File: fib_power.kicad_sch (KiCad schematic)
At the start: 44 parts, among them U2 TPS56428DDA, U202 TLV75733PDBV, U204 TPS56428DDA, U205 TPS56428DDA

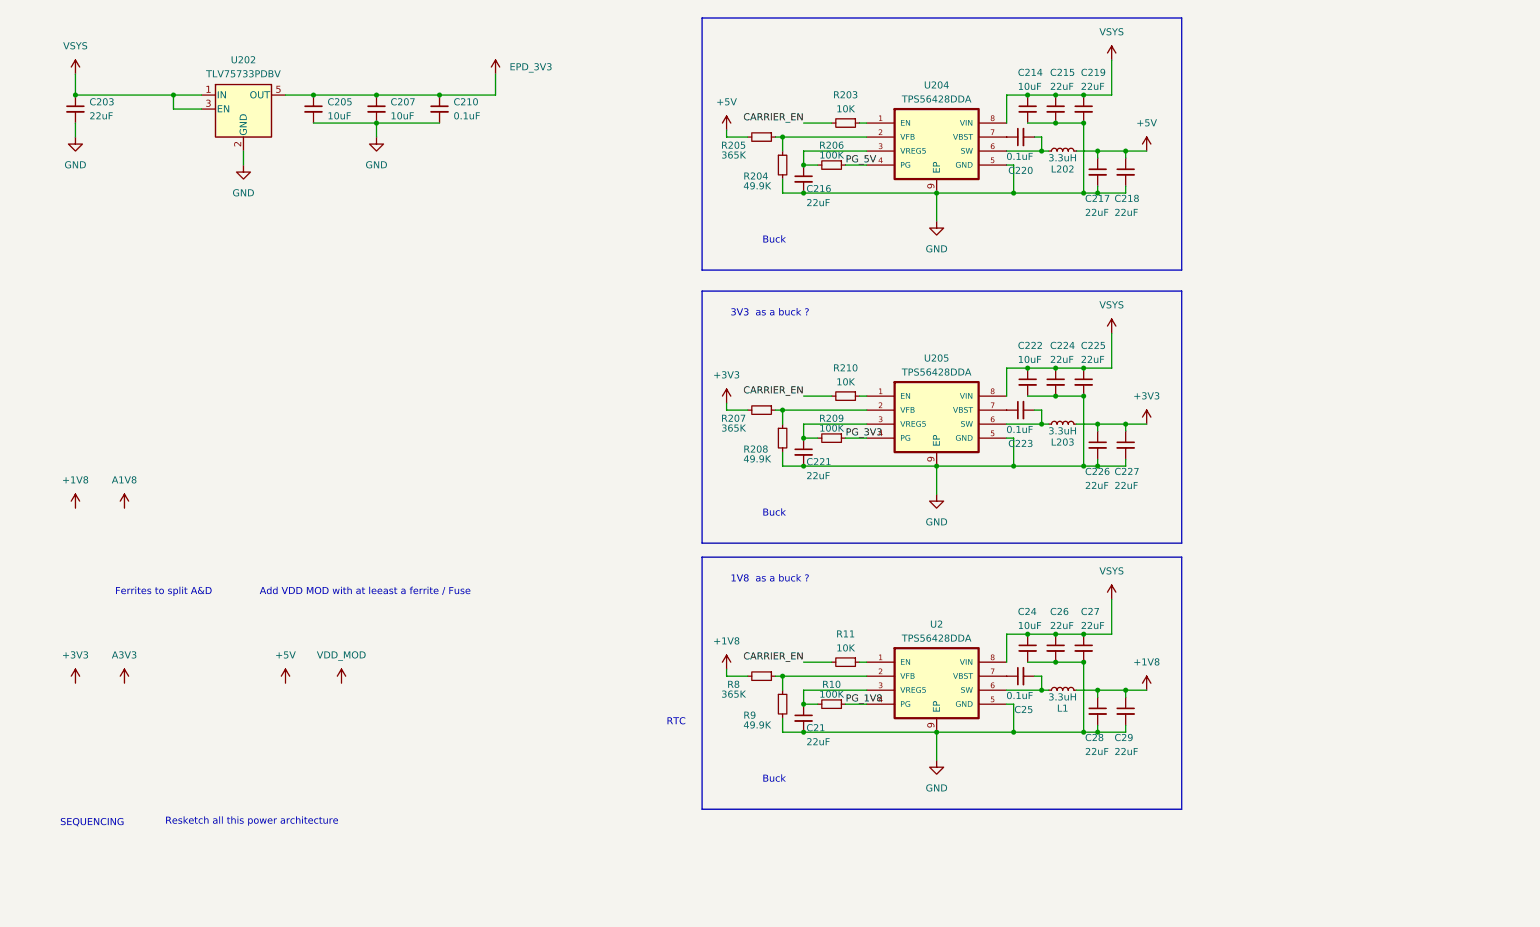
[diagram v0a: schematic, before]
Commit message: replaced 1v8 buck with ldo, added startup circuit, added footprints for eink connectors
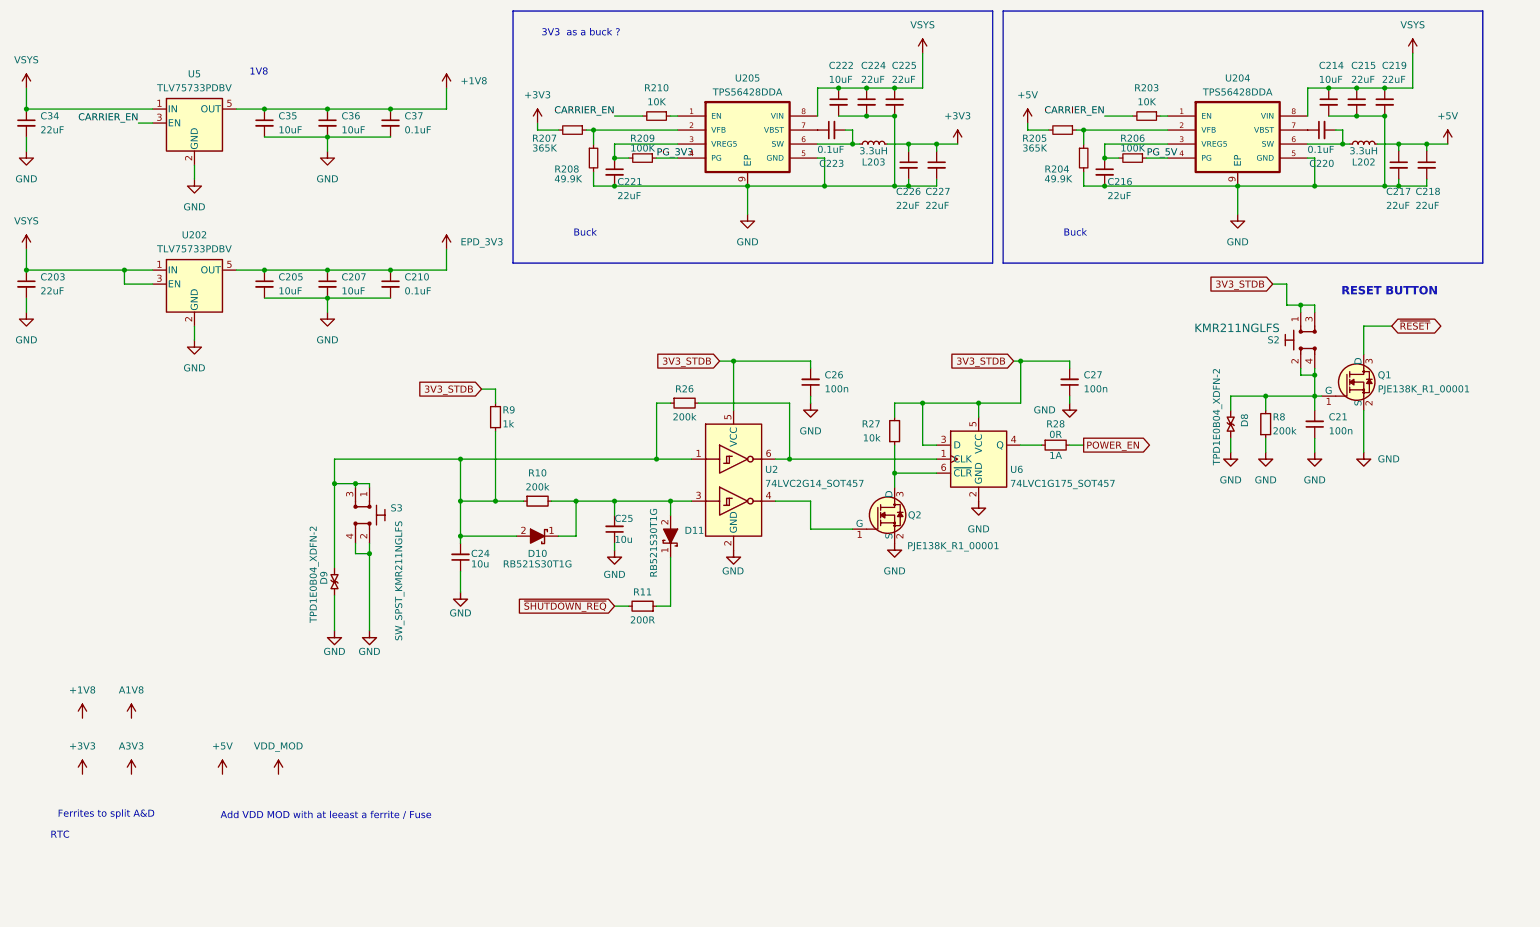
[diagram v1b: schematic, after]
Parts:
- removed C21, C26, C27, C29: 22uF, Capacitor_SMD:C_0805_2012Metric, symbol Device:C_Small
- removed C24: 10uF, Capacitor_SMD:C_0603_1608Metric, symbol Device:C_Small
- removed C25: 0.1uF, Capacitor_SMD:C_0402_1005Metric, symbol Device:C_Small
- removed C28: 22uF, Capacitor_SMD:C_0603_1608Metric, symbol Device:C_Small
- removed L1: 3.3uH, Inductor_SMD:L_Coilcraft_XAL4030-XXX, symbol Device:L_Small
- removed R10: 100K, Resistor_SMD:R_0402_1005Metric, symbol Device:R_Small
- removed R11: 10K, Resistor_SMD:R_0402_1005Metric, symbol Device:R_Small
- removed R8: 365K, Resistor_SMD:R_0402_1005Metric, symbol Device:R_Small
- removed R9: 49.9K, Resistor_SMD:R_0402_1005Metric, symbol Device:R_Small
- removed U2: TPS56428DDA, Fibel2:TPS56428DDA, symbol Fibel2:TPS56428DDA
- added C21, C26, C27: C_100n_0402, antmicro-footprints:C_0402_1005Metric, symbol antmicroCapacitors0402:C_100n_0402
- added C24, C25: C_10u_0402, antmicro-footprints:C_0402_1005Metric, symbol antmicroCapacitors0402:C_10u_0402
- added C34: 22uF, Capacitor_SMD:C_0805_2012Metric, symbol Device:C_Small
- added C35, C36: 10uF, Capacitor_SMD:C_0603_1608Metric, symbol Device:C_Small
- added C37: 0.1uF, Capacitor_SMD:C_0402_1005Metric, symbol Device:C_Small
- added D10, D11: RB521S30T1G, antmicro-footprints:SOD-523, symbol antmicroDiodesRectifiersSingle:RB521S30T1G
- added D8, D9: TPD1E0B04_XDFN-2, antmicro-footprints:XDFN-2_1x0.60mm, symbol antmicroTVSDiodes:TPD1E0B04_XDFN-2
- added Q1, Q2: PJE138K, antmicro-footprints:SOT-523, symbol antmicroTransistorsFETsMOSFETsSingle:PJE138K
- added R10, R26, R8: R_200k_0402, antmicro-footprints:R_0402_1005Metric, symbol antmicroResistors0402:R_200k_0402
- added R11: R_200R_0402, antmicro-footprints:R_0402_1005Metric, symbol antmicroResistors0402:R_200R_0402
- added R27: R_10k_0402, antmicro-footprints:R_0402_1005Metric, symbol antmicroResistors0402:R_10k_0402
- added R28: R_0R_0402, antmicro-footprints:R_0402_1005Metric, symbol antmicroResistors0402:R_0R_0402
- added R9: R_1k_0402, antmicro-footprints:R_0402_1005Metric, symbol antmicroResistors0402:R_1k_0402
- added S2, S3: SW_SPST_KMR211NGLFS, antmicro-footprints:SW_KMR211NGLFS_SMD, symbol antmicroPushbuttonSwitches:SW_KMR211NGLFS_SMD
- added U2: 74LVC2G14_SOT457, antmicro-footprints:SOT-23-6, symbol antmicroLogicBuffersDriversReceiversTransceivers:74LVC2G14_SOT457
- added U5: TLV75733PDBV, Package_TO_SOT_SMD:SOT-23-5, symbol Regulator_Linear:TLV75733PDBV
- added U6: 74LVC1G175_SOT457, antmicro-footprints:SOT-23-6, symbol antmicroLogicGatesandInverters:74LVC1G175_SOT457
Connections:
- net +1V8: now also C35.1, C36.1, C37.1, U5.5 (OUT)
- net CARRIER_EN: now also U5.3 (EN)
- net GND: now also C21.1, C24.1, C25.1, C26.1, C27.1, C34.2, C35.2, C36.2, C37.2, D8.1, D9.1, Q1.2 (S), Q2.2 (S), R8.1, S3.2, S3.4, U2.2 (GND), U5.2 (GND), U6.2 (GND)
- net VSYS: now also C34.1, U5.1 (IN)
- new net: C21.2, D8.2, Q1.1 (G), R8.2, S2.2, S2.4
- new net: C24.2, D10.2, D9.2, R10.1, R26.1, R9.1, S3.1, S3.3, U2.1
- new net: R26.2, U2.6, U6.1 (CLK)
- new net: R28.1, U6.4 (Q)
- new net: Q2.3 (D), R27.1, U6.6 (~{CLR})
- new net: C25.2, D10.1, D11.2, R10.2, U2.3
- new net: Q2.1 (G), U2.4
- new net: D11.1, R11.1
- new net 3V3_STDB: C26.2, C27.2, R27.2, R9.2, S2.1, S2.3, U2.5 (VCC), U6.3 (D), U6.5 (VCC)
- new net POWER_EN: R28.2
- new net ~{RESET}: Q1.3 (D)
- new net ~{SHUTDOWN_REQ}: R11.2
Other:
- note added: "1V8"
- note added: "RESET BUTTON"
- note removed: "1V8 as a buck ?"
- note removed: "Resketch all this power architecture"
- note removed: "SEQUENCING"
- moved on the sheet: C203, C205, C207, C210, C214, C215, C216, C217, C218, C219, C220, C221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

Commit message: added all missing footprints, fixed library & footprint links, did layout out 99% of components, all that's left is rtc(?), peripherals, routing & lengthmatching and final sanity checks
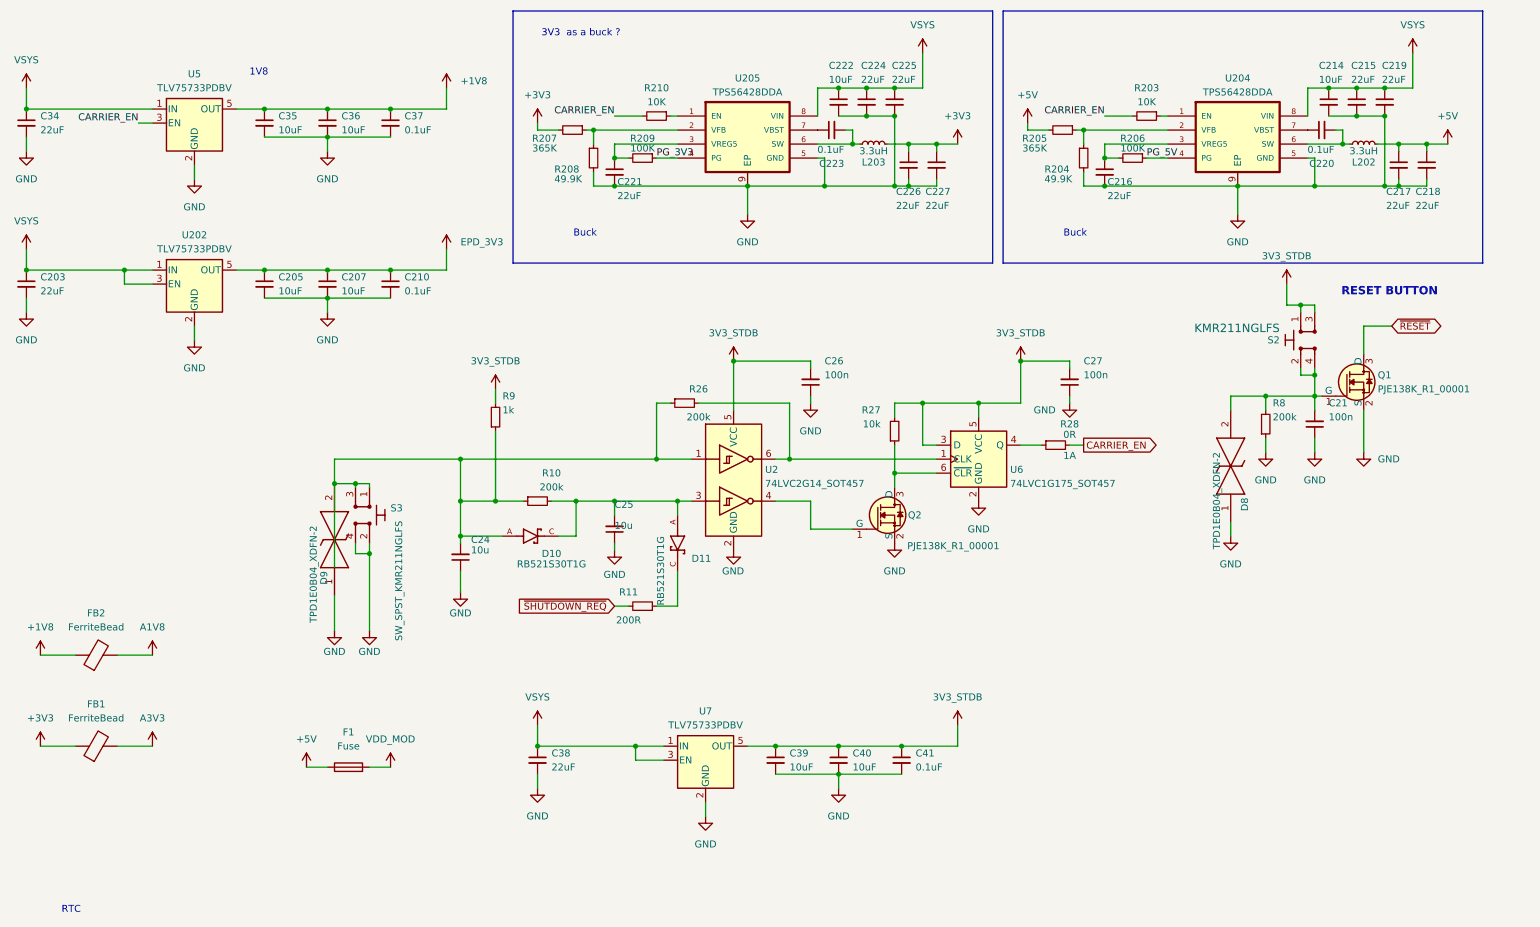
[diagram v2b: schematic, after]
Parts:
- added C38: 22uF, Capacitor_SMD:C_0805_2012Metric, symbol Device:C_Small
- added C39, C40: 10uF, Capacitor_SMD:C_0603_1608Metric, symbol Device:C_Small
- added C41: 0.1uF, Capacitor_SMD:C_0402_1005Metric, symbol Device:C_Small
- added F1: Fuse, Fibel2:Fuse_1206, symbol Device:Fuse
- added FB1, FB2: FerriteBead, Fibel2:Ferrite_1206, symbol Device:FerriteBead
- added U7: TLV75733PDBV, Package_TO_SOT_SMD:SOT-23-5, symbol Regulator_Linear:TLV75733PDBV
- C21, C26, C27: value C_100n_0402 -> C_Small_Rota; footprint antmicro-footprints:C_0402_1005Metric -> Capacitor_SMD:C_0402_1005Metric; symbol antmicroCapacitors0402:C_100n_0402 -> Fibel2:C_Small_Rota
- C24, C25: value C_10u_0402 -> C_Small_Rota; footprint antmicro-footprints:C_0402_1005Metric -> Capacitor_SMD:C_0402_1005Metric; symbol antmicroCapacitors0402:C_10u_0402 -> Fibel2:C_Small_Rota
- D10, D11: footprint antmicro-footprints:SOD-523 -> Fibel2:RB521S30T1G; symbol antmicroDiodesRectifiersSingle:RB521S30T1G -> Fibel2:RB521S30T1G; Availability (none) -> In Stock; Check_prices (none) -> https://www.snapeda.com/parts/BAT54WT-7/Diodes+Inc./view-pa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; Description_1 (none) -> Diodes Inc BAT54WT-7, SMT Schottky Diode, 30V 200mA, 5ns, 2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; MANUFACTURER (none) -> DIODES; MAXIMUM_PACKAGE_HEIGHT (none) -> 0.65mm; MF (none) -> Diodes Inc.; MP (none) -> BAT54WT-7; PARTREV (none) -> 3-2; Package (none) -> SOD-523 Diodes Inc.; Price (none) -> None; Purchase-URL (none) -> https://www.snapeda.com/api/url_track_click_mouser/?unipart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; STANDARD (none) -> IPC-7351B; SnapEDA_Link (none) -> https://www.snapeda.com/parts/BAT54WT-7/Diodes+Inc./view-pa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
- D8, D9: footprint antmicro-footprints:XDFN-2_1x0.60mm -> TPD1E0B04DPYT; symbol antmicroTVSDiodes:TPD1E0B04_XDFN-2 -> Fibel2:TPD1E0B04DPYT; Height (none) -> 0.45; Manufacturer_Name (none) -> Texas Instruments; Manufacturer_Part_Number (none) -> TPD1E0B04DPYT; Mouser Part Number (none) -> 595-TPD1E0B04DPYT; Mouser Price/Stock (none) -> https://www.mouser.co.uk/ProductDetail/Texas-Instruments/TP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
- Q1, Q2: value PJE138K -> PJE138K_2; footprint antmicro-footprints:SOT-523 -> Fibel2:SOT-523; symbol antmicroTransistorsFETsMOSFETsSingle:PJE138K -> Fibel2:PJE138K_2
- R10, R26, R8: value R_200k_0402 -> R_Small_Rota; footprint antmicro-footprints:R_0402_1005Metric -> Resistor_SMD:R_0402_1005Metric; symbol antmicroResistors0402:R_200k_0402 -> Fibel2:R_Small_Rota
- R11: value R_200R_0402 -> R_Small_Rota; footprint antmicro-footprints:R_0402_1005Metric -> Resistor_SMD:R_0402_1005Metric; symbol antmicroResistors0402:R_200R_0402 -> Fibel2:R_Small_Rota
- R27: value R_10k_0402 -> R_Small_Rota; footprint antmicro-footprints:R_0402_1005Metric -> Resistor_SMD:R_0402_1005Metric; symbol antmicroResistors0402:R_10k_0402 -> Fibel2:R_Small_Rota
- R28: value R_0R_0402 -> R_Small_Rota; footprint antmicro-footprints:R_0402_1005Metric -> Resistor_SMD:R_0402_1005Metric; symbol antmicroResistors0402:R_0R_0402 -> Fibel2:R_Small_Rota
- R9: value R_1k_0402 -> R_Small_Rota; footprint antmicro-footprints:R_0402_1005Metric -> Resistor_SMD:R_0402_1005Metric; symbol antmicroResistors0402:R_1k_0402 -> Fibel2:R_Small_Rota
- S2, S3: footprint antmicro-footprints:SW_KMR211NGLFS_SMD -> Fibel2:KMR211NGLFS; symbol antmicroPushbuttonSwitches:SW_KMR211NGLFS_SMD -> Fibel2:SW_KMR211NGLFS_SMD
- U2: footprint antmicro-footprints:SOT-23-6 -> Fibel2:SOT-23-6; symbol antmicroLogicBuffersDriversReceiversTransceivers:74LVC2G14_SOT457 -> Fibel2:74LVC2G14_SOT457
- U6: footprint antmicro-footprints:SOT-23-6 -> Fibel2:SOT-23-6; symbol antmicroLogicGatesandInverters:74LVC1G175_SOT457 -> Fibel2:74LVC1G175_SOT457
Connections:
- net POWER_EN is gone; now on net CARRIER_EN: R28.2
- net +1V8: now also FB2.1
- net +3V3: now also FB1.1
- net +5V: now also F1.1
- net 3V3_STDB: now also C39.1, C40.1, C41.1, U7.5 (OUT)
- net A1V8: now also FB2.2
- net A3V3: now also FB1.2
- net GND: now also C38.2, C39.2, C40.2, C41.2, U7.2 (GND)
- net VDD_MOD: now also F1.2
- net VSYS: now also C38.1, U7.1 (IN), U7.3 (EN)
- net at C24.2, D9.2, R10.1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: now also D10.A; no longer D10.2
- net at C25.2, R10.2, U2.3: now also D10.C, D11.A; no longer D10.1, D11.2
- net at R11.1: now also D11.C; no longer D11.1
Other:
- note removed: "Add VDD MOD with at leeast a ferrite / Fuse"
- note removed: "Ferrites to split A&D"

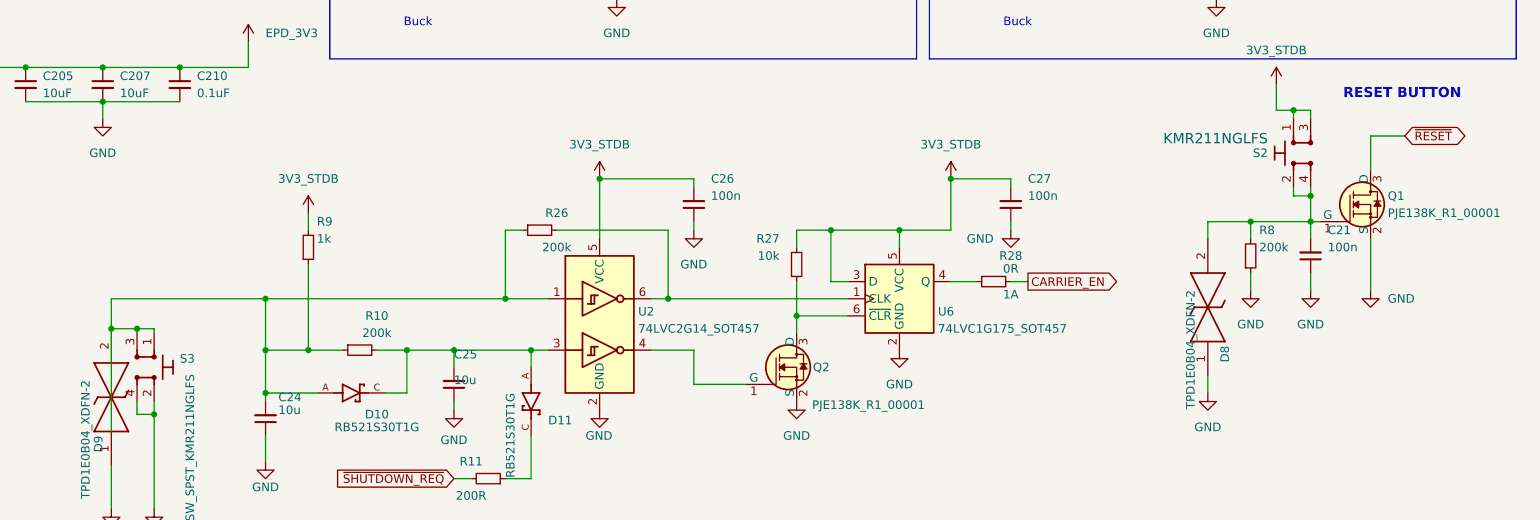
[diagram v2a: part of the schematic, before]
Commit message: did length tuning, routing of final submodules and most of power routing
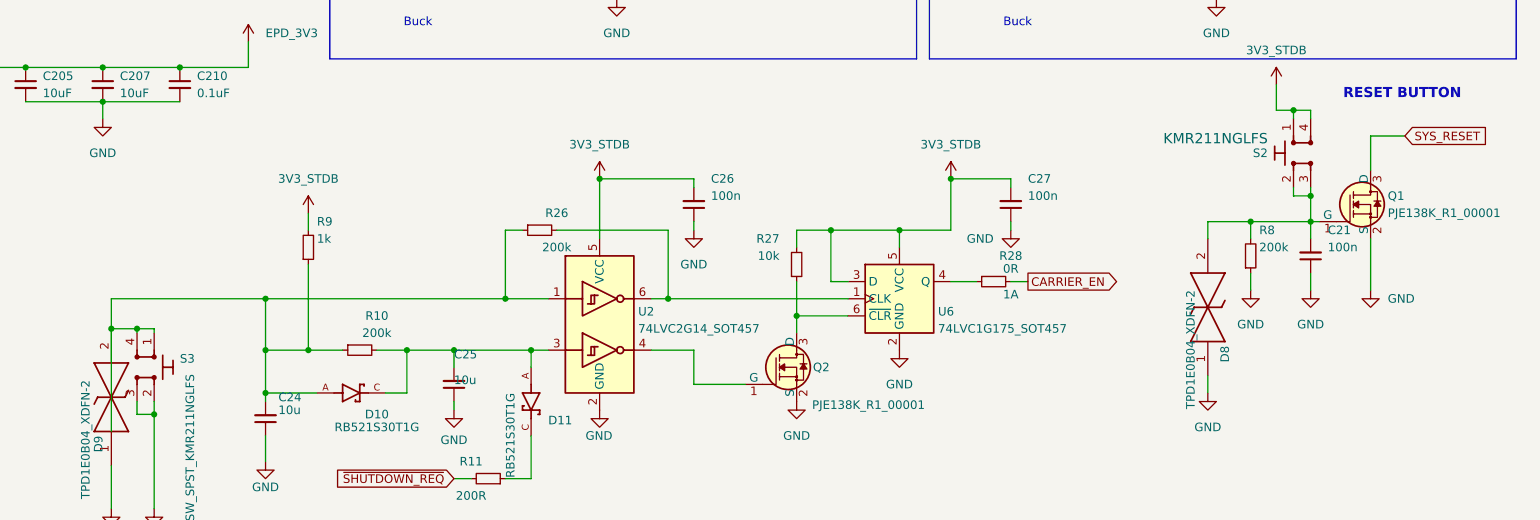
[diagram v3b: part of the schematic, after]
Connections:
- net 3V3_STDB: now also S2.4; no longer S2.3
- net GND: now also S3.3; no longer S3.4
- net at C21.2, D8.2, Q1.1 (G)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: now also S2.3; no longer S2.4
- net at C24.2, D10.A, D9.2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: now also S3.4; no longer S3.3
- net ~{RESET} renamed SYS_RESET
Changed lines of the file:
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@@
 		)
 		(property "Intersheetrefs" "${INTERSHEET_REFS}"
-			(at 108.3793 121.8406 0)
+			(at 107.8072 121.92 0)
 			(effects
 				(font
@@
 				)
 				(justify right)
-				(hide yes)
-			)
-		)
-	)
-	(global_label "~{RESET}"
-		(shape bidirectional)
-		(at 266.7 71.12 0)
-		(effects
-			(font
-				(size 1.27 1.27)
-			)
-			(justify left)
-		)
-		(property "Intersheetrefs" "${INTERSHEET_REFS}"
-			(at 276.86 71.12 0)
-			(effects
-				(font
-					(size 1.27 1.27)
-				)
-				(justify left)
 				(hide yes)
 			)
@@
 			(effects
 				(font
+					(size 1.27 1.27)
+				)
+				(justify left)
+				(hide yes)
+			)
+		)
+	)
+	(global_label "SYS_RESET"
+		(shape input)
+		(at 266.7 71.12 0)
+		(fields_autoplaced yes)
+		(effects
+			(font
+				(size 1.27 1.27)
+			)
+			(justify left)
+		)
+		(property "Intersheetrefs" "${INTERSHEET_REFS}"
+			(at 279.9055 71.12 0)
+			(effects
+				(font
